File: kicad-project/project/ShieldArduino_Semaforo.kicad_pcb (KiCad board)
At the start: 2 copper layers, 68.6 x 53.3 mm, 92 parts, among them IC1 TPS563200DDCR, IC2 TPS563200DDCR, J1 Conn_01x01, J10 Conn_01x01, J11 Conn_01x01, J12 Conn_01x01, J13 Conn_01x01, J14 Conn_01x01, J15 Conn_01x01, J2 Conn_01x01, J3 Conn_01x01, J4 Conn_01x01, J5 Conn_01x01, J6 Conn_01x01, J7 Conn_01x01, J8 Conn_01x01, J9 Conn_01x01, K1 RELAY, P1 Power, P2 Analog, P3 Digital, P4 Digital, P5 CONN_01X01, P6 CONN_01X01, P7 CONN_01X01, P8 CONN_01X01, Q1 PMOS, Q2 NMOS, Q3 NMOS, Q4 NMOS, Q5 NMOS, U1 MCP2542FD-E/MF, U2 LM321

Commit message: xd
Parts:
- removed C10, C11: 22u, Capacitor_SMD:C_0603_1608Metric_Pad1.08x0.95mm_HandSolder
- removed C12, C3, C5: 1uF, Capacitor_SMD:C_0603_1608Metric_Pad1.08x0.95mm_HandSolder
- removed C6: 10u, Capacitor_SMD:C_0805_2012Metric_Pad1.18x1.45mm_HandSolder
- removed C8: 10uf, Capacitor_SMD:C_0805_2012Metric_Pad1.18x1.45mm_HandSolder
- removed C9: 100n 280mOhm, Capacitor_SMD:C_0805_2012Metric_Pad1.18x1.45mm_HandSolder
- removed D3: Diode TVS 12V, Diode_SMD:D_SOD-323F
- removed F1: 3A, Fuse:Fuse_0603_1608Metric_Pad1.05x0.95mm_HandSolder
- removed the F3 at (124.2, 92.7)
- removed the F3 at (131.6, 99.3)
- removed IC1: TPS563200DDCR, footprint:TPS563200DDCR
- removed R12: 56.2k 50mW, Resistor_SMD:R_0603_1608Metric_Pad0.98x0.95mm_HandSolder
- removed R13: 10k 50mW, Resistor_SMD:R_0603_1608Metric_Pad0.98x0.95mm_HandSolder
- removed REF**: KiCad-Logo2_8mm_SilkScreen, Symbol:KiCad-Logo2_8mm_SilkScreen
- removed REF**: OSHW-Logo2_14.6x12mm_SilkScreen, Symbol:OSHW-Logo2_14.6x12mm_SilkScreen
- removed TP1, TP2: TestPoint_Small, TestPoint:TestPoint_Pad_D1.0mm
- added C134: 1uF, Capacitor_SMD:C_0603_1608Metric_Pad1.08x0.95mm_HandSolder, F.Cu at (133.4, 86.8)
- added C135: 1uF, Capacitor_SMD:C_0603_1608Metric_Pad1.08x0.95mm_HandSolder, F.Cu at (133.4, 85.2)
- added C136: 1uF, Capacitor_SMD:C_0603_1608Metric_Pad1.08x0.95mm_HandSolder, F.Cu at (94.5, 100.9)
- added D16: Diode TVS 12V, Diode_SMD:D_SOD-323F, F.Cu at (133.4, 83.4)
- added F3: 3A, Fuse:Fuse_0603_1608Metric_Pad1.05x0.95mm_HandSolder, F.Cu at (132.1, 91.4)
- added F4: 1A, Fuse:Fuse_0603_1608Metric_Pad1.05x0.95mm_HandSolder, F.Cu at (94.5, 103.4)
- added TP12: TestPoint_Small, TestPoint:TestPoint_Pad_D1.0mm, F.Cu at (98.2, 102.4)
- IC2: footprint footrpint:TPS563200DDCR -> footprint:TPS563200DDCR
- moved F2 35.7 mm to (101.2, 95.8)
- moved L1 9.36 mm to (127.8, 108.1)
- moved C120 8.01 mm to (128.9, 98.8)
- moved IC2 8.01 mm to (129.1, 91.1)
- moved C119 8.01 mm to (129.0, 96.1)
- moved C121 8.01 mm to (126.7, 86.7)
- moved C122 8.01 mm to (126.2, 100.2)
- moved C123 8.01 mm to (124.0, 100.2)
- moved R165 8.01 mm to (127.0, 82.5)
- moved R166 8.01 mm to (127.0, 84.4)
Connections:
- net +12V renamed Net-(IC2-EN)
- C122 pad 1: /Power/5V/5V_unfused -> /5V_unfused
- C123 pad 1: /Power/5V/5V_unfused -> /5V_unfused
- J10 pad 1: /UART_RX -> /EX_CAN-
- J11 pad 1: /UART_TX -> / relay_in
- L1 pad 1: Net-(IC1-SW) -> Net-(IC2-SW)
- R165 pad 2: /Power/5V/5V_unfused -> /5V_unfused
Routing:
- net 12V_IN: track 6.05 -> 0.00 mm
- net /12V_in_protected: track 0.00 -> 3.20 mm
- net /Power/5V/5V_unfused: track 2.77 -> 0.00 mm
- net /5V_unfused: track 0.00 -> 1.84 mm
- added copper zone on F.Cu, net /12V_in_protected
- removed copper zone on F.Cu, net 12V_IN

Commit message: test
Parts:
- turned D16 to 180 degrees
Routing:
- net /5V_unfused: track 1.84 -> 33.5 mm
- net GND: track 9.98 -> 0.00 mm
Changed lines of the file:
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@@
 	(footprint "Diode_SMD:D_SOD-323F"
 		(layer "F.Cu")
-		(at 133.398 83.365)
+		(at 133.398 83.365 180)
 		(descr "SOD-323F http://www.nxp.com/documents/outline_drawing/SOD323F.pdf")
 		(tags "SOD-323F")
@@
 		)
 		(property "Datasheet" "https://www.mouser.pl/ProductDetail/Diodes-Incorporated/SD12C-7?qs=EBDBlbfErPxugjAb5VaoMA%3D%3D"
-			(at 0 0 0)
+			(at 0 0 180)
 			(unlocked yes)
 			(layer "F.Fab")
@@
 		)
 		(property "Description" "Bidirectional transient-voltage-suppression diode"
-			(at 0 0 0)
+			(at 0 0 180)
 			(unlocked yes)
 			(layer "F.Fab")
@@
 		(attr smd)
 		(fp_line
-			(start -1.61 -0.85)
-			(end -1.61 0.85)
+			(start -1.61 0.85)
+			(end 1.05 0.85)
 			(stroke
 				(width 0.12)
@@
 		)
 		(fp_line
-			(start -1.61 0.85)
-			(end 1.05 0.85)
+			(start -1.61 -0.85)
+			(end -1.61 0.85)
 			(stroke
 				(width 0.12)
@@
 		)
 		(fp_line
-			(start -1.6 -0.95)
-			(end -1.6 0.95)
+			(start 1.6 -0.95)
+			(end 1.6 0.95)
 			(stroke
 				(width 0.05)
@@
 		)
 		(fp_line
-			(start -1.6 -0.95)
-			(end 1.6 -0.95)
+			(start -1.6 0.95)
+			(end 1.6 0.95)
 			(stroke
 				(width 0.05)
@@
 		)
 		(fp_line
-			(start -1.6 0.95)
-			(end 1.6 0.95)
+			(start -1.6 -0.95)
+			(end 1.6 -0.95)
 			(stroke
 				(width 0.05)
@@
 		)
 		(fp_line
-			(start 1.6 -0.95)
-			(end 1.6 0.95)
+			(start -1.6 -0.95)
+			(end -1.6 0.95)
 			(stroke
 				(width 0.05)
@@
 		)
 		(fp_line
-			(start -0.9 -0.7)
-			(end 0.9 -0.7)
+			(start 0.9 0.7)
+			(end -0.9 0.7)
 			(stroke
 				(width 0.1)
@@
 		)
 		(fp_line
-			(start -0.9 0.7)
-			(end -0.9 -0.7)
+			(start 0.9 -0.7)
+			(end 0.9 0.7)
 			(stroke
 				(width 0.1)
@@
 		)
 		(fp_line
-			(start -0.3 -0.35)
-			(end -0.3 0.35)
+			(start 0.2 0.35)
+			(end -0.3 0)
 			(stroke
 				(width 0.1)
@@
 		)
 		(fp_line
-			(start -0.3 0)
-			(end -0.5 0)
+			(start 0.2 0)
+			(end 0.45 0)
 			(stroke
 				(width 0.1)
@@
 		)
 		(fp_line
-			(start -0.3 0)
-			(end 0.2 -0.35)
+			(start 0.2 -0.35)
+			(end 0.2 0.35)
 			(stroke
 				(width 0.1)
@@
 		)
 		(fp_line
-			(start 0.2 -0.35)
-			(end 0.2 0.35)
+			(start -0.3 0)
+			(end 0.2 -0.35)
 			(stroke
 				(width 0.1)
@@
 		)
 		(fp_line
-			(start 0.2 0)
-			(end 0.45 0)
+			(start -0.3 0)
+			(end -0.5 0)
 			(stroke
 				(width 0.1)
@@
 		)
 		(fp_line
-			(start 0.2 0.35)
-			(end -0.3 0)
+			(start -0.3 -0.35)
+			(end -0.3 0.35)
 			(stroke
 				(width 0.1)
@@
 		)
 		(fp_line
-			(start 0.9 -0.7)
-			(end 0.9 0.7)
+			(start -0.9 0.7)
+			(end -0.9 -0.7)
 			(stroke
 				(width 0.1)
@@
 		)
 		(fp_line
-			(start 0.9 0.7)
-			(end -0.9 0.7)
+			(start -0.9 -0.7)
+			(end 0.9 -0.7)
 			(stroke
 				(width 0.1)
@@
 		)
 		(pad "1" smd roundrect
-			(at -1.1 0)
+			(at -1.1 0 180)
 			(size 0.5 0.5)
 			(layers "F.Cu" "F.Mask" "F.Paste")
@@
 		)
 		(pad "2" smd roundrect
-			(at 1.1 0)
+			(at 1.1 0 180)
 			(size 0.5 0.5)
 			(layers "F.Cu" "F.Mask" "F.Paste")
@@
 		)
 	)
-	(segment
-		(start 123.248 91.75875)
-		(end 123.398 91.90875)
-		(width 0.2)
-		(layer "F.Cu")
-		(net 2)
-	)
-	(segment
-		(start 126.073 84.440155)
-		(end 123.8855 84.440155)
-		(width 0.2)
-		(layer "F.Cu")
-		(net 2)
-	)
-	(segment
-		(start 123.8855 84.440155)
-		(end 123.248 85.077655)
-		(width 0.2)
-		(layer "F.Cu")
-		(net 2)
-	)
-	(segment
-		(start 123.248 85.077655)
-		(end 123.248 91.75875)
-		(width 0.2)
-		(layer "F.Cu")
-		(net 2)
-	)
 	(via
 		(at 126.498 97.45875)
@@
 	)
 	(segment
+		(start 121.398 83.965)
+		(end 121.398 98.477655)
+		(width 0.2)
+		(layer "F.Cu")
+		(net 58)
+	)
+	(segment
+		(start 124.685499 82.490155)
+		(end 122.872845 82.490155)
+		(width 0.2)
+		(layer "F.Cu")
+		(net 58)
+	)
+	(segment
 		(start 124.685499 82.490155)
 		(end 124.529327 82.646327)
@@
 	)
 	(segment
+		(start 124.023 107.340155)
+		(end 124.773 108.090155)
+		(width 0.5)
+		(layer "F.Cu")
+		(net 58)
+	)
+	(segment
+		(start 121.398 98.477655)
+		(end 124.023 101.102655)
+		(width 0.2)
+		(layer "F.Cu")
+		(net 58)
+	)
+	(segment
+		(start 122.872845 82.490155)
+		(end 121.398 83.965)
+		(width 0.2)
+		(layer "F.Cu")
+		(net 58)
+	)
+	(segment
 		(start 126.0855 82.490155)
 		(end 124.685499 82.490155)
@@
 		(layer "F.Cu")
 		(net 58)
+	)
+	(segment
+		(start 126.223 101.102655)
+		(end 124.023 101.102655)
+		(width 0.5)
+		(layer "F.Cu")
+		(net 58)
+	)
+	(segment
+		(start 124.023 101.102655)
+		(end 124.023 107.340155)
+		(width 0.5)
+		(layer "F.Cu")
+		(net 58)

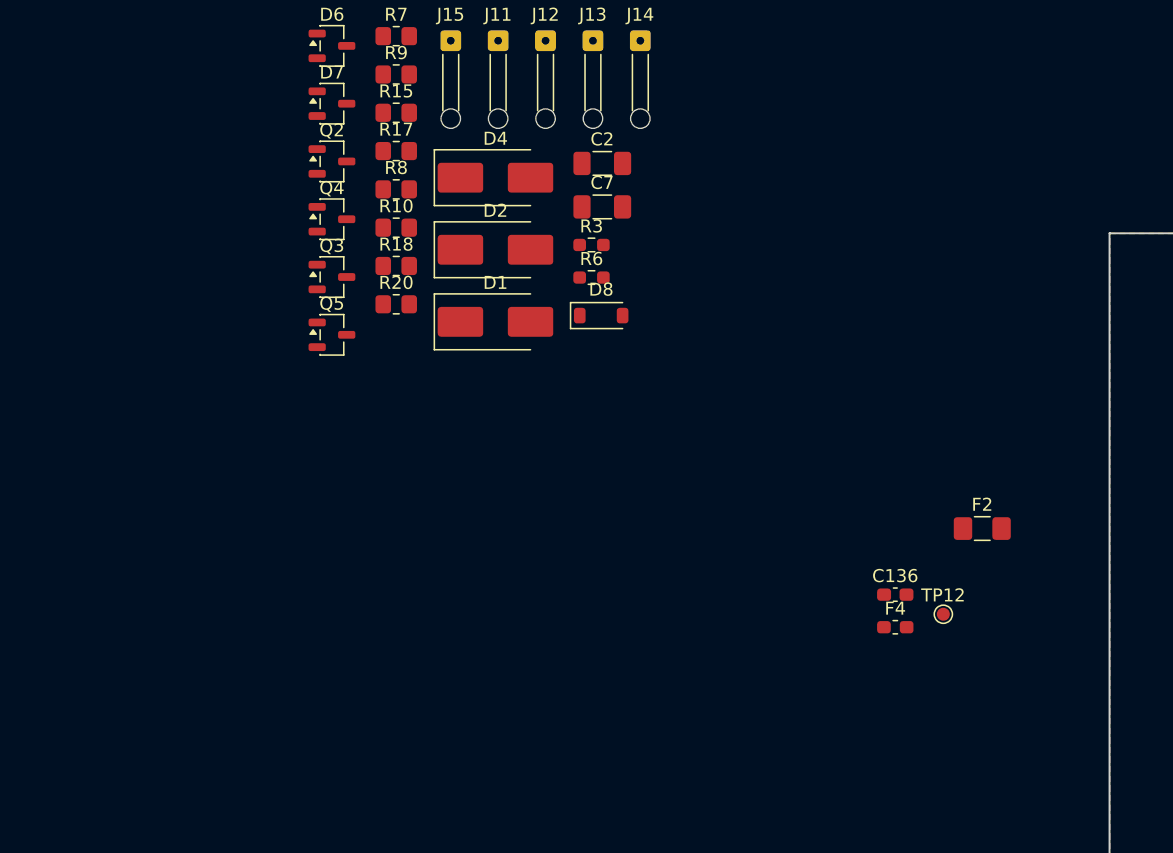
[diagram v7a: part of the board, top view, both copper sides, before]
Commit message: kicad-relay_transistor_pcb-layout
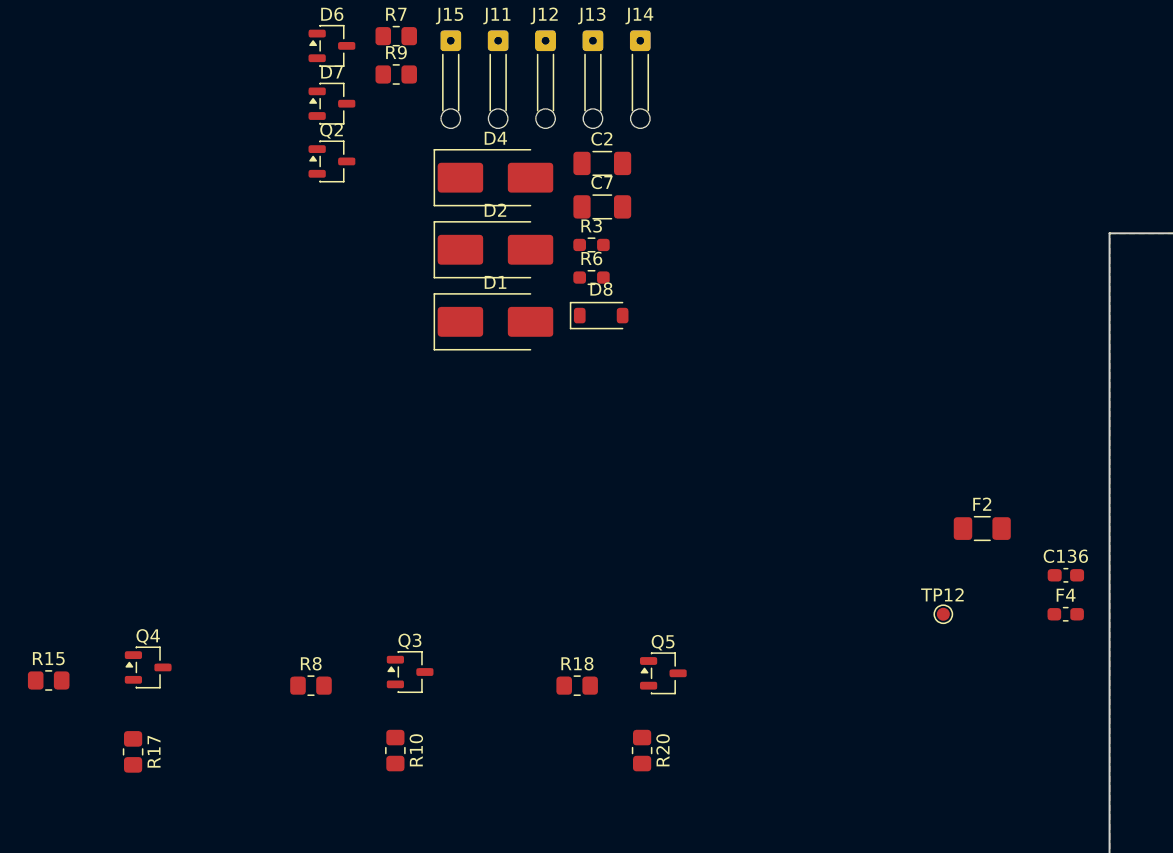
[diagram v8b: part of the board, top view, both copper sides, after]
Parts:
- moved R15 51.3 mm to (29.3, 107.5)
- moved R17 50.5 mm to (35.8, 113.0), turned to -90 degrees
- moved R10 40.3 mm to (56.0, 112.9), turned to -90 degrees
- moved R20 39.2 mm to (75.0, 112.9), turned to -90 degrees
- moved R8 38.8 mm to (49.5, 107.9)
- moved Q4 37.3 mm to (37.0, 106.5)
- moved Q5 36.5 mm to (76.6, 106.9)
- moved R18 35.2 mm to (70.0, 107.9)
- moved Q3 31.0 mm to (57.1, 106.8)
- moved C136 13.2 mm to (107.6, 99.4)
- moved F4 13.2 mm to (107.6, 102.4)
